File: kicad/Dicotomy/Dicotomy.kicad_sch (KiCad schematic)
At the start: 17 parts, among them J1 Conn_01x02_Pin, J2 Conn_01x04_Pin, J3 Conn_01x04_Socket, J4 Conn_01x02_Socket, Q1 Q_PNP, Q2 NPN, Q3 NPN, Q4 NPN, U1 WEMO S2 mini, U2 AC PWR SSR

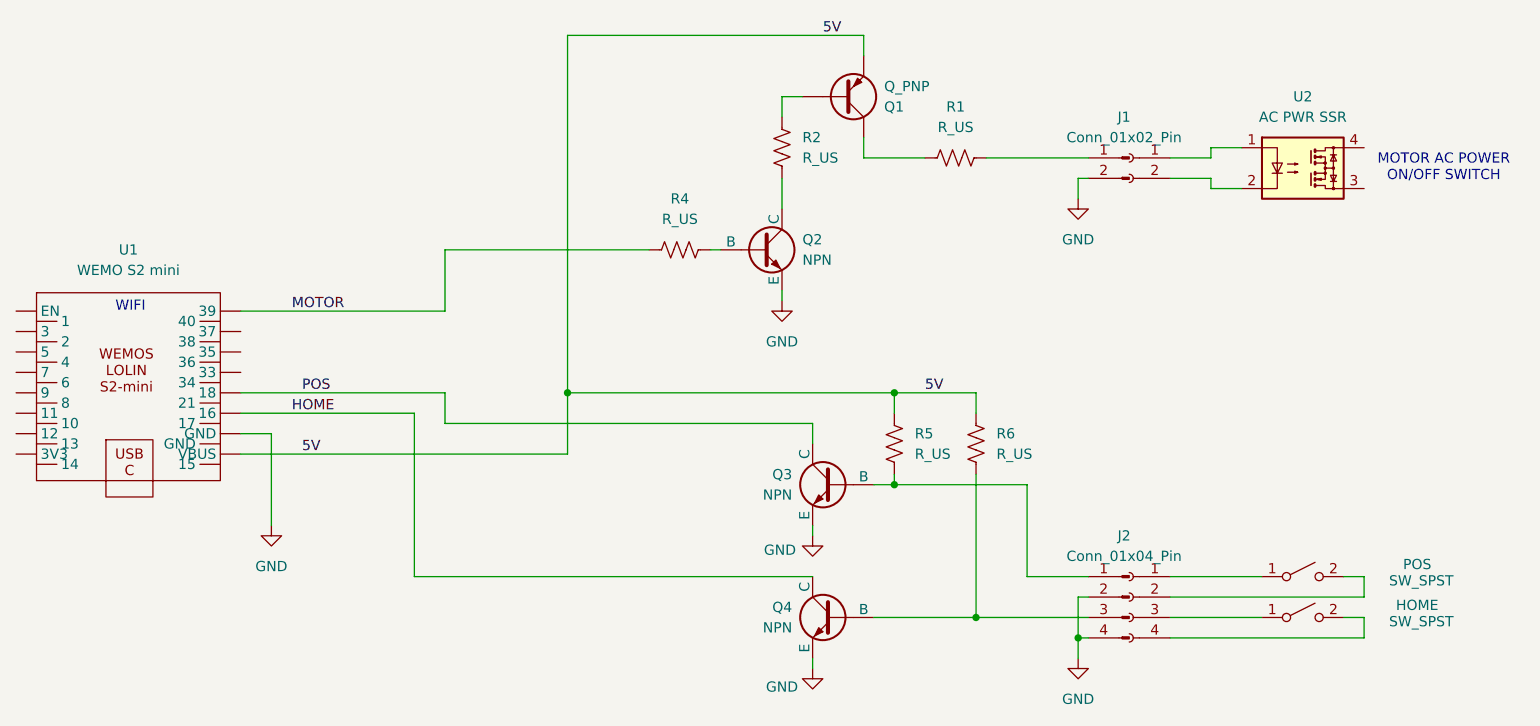
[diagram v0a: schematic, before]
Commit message: Update schematic with tran types and resistor values Created add_rotate.md requirements which are additions to the code_onoff.md requirements and used AI to create code_rotate.ino The basis of the code works, but fails to complete homing sequence on the bench while manually triggering switches, even with default home offset of 0 degrees. Added debug print statements TODO: Debug more
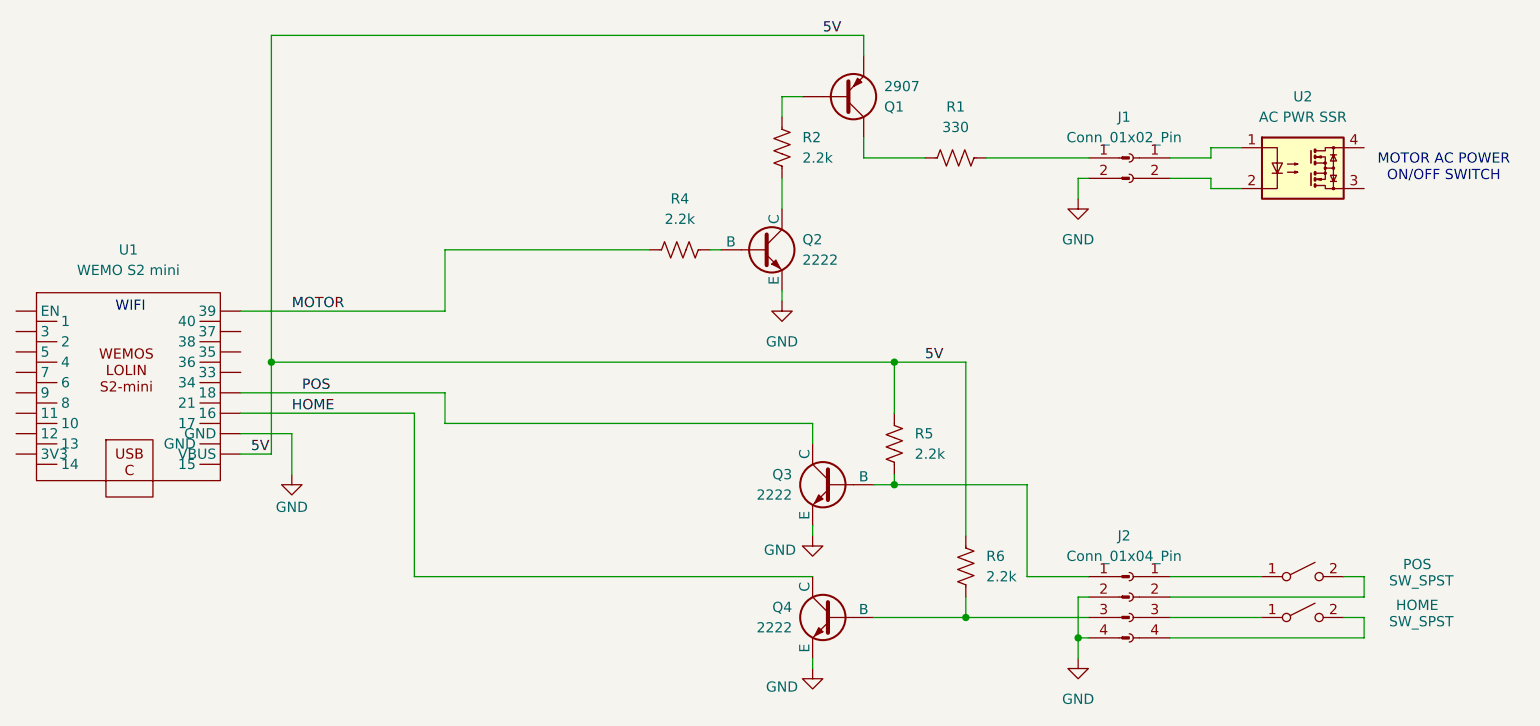
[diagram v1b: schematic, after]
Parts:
- Q1: value Q_PNP -> 2907
- Q2, Q3, Q4: value NPN -> 2222
- R1: value R_US -> 330
- R2, R4, R5, R6: value R_US -> 2.2k
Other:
- moved on the sheet: R6
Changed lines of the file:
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@@
 	)
 	(junction
-		(at 129.54 107.95)
+		(at 170.18 104.14)
 		(diameter 0)
 		(color 0 0 0 0)
 	)
 	(junction
-		(at 170.18 107.95)
+		(at 179.07 135.89)
 		(diameter 0)
 		(color 0 0 0 0)
 	)
 	(junction
-		(at 180.34 135.89)
+		(at 92.71 104.14)
 		(diameter 0)
 		(color 0 0 0 0)
@@
 	(wire
 		(pts
-			(xy 129.54 107.95) (xy 170.18 107.95)
-		)
-		(stroke
-			(width 0)
-			(type default)
-		)
-	)
-	(wire
-		(pts
 			(xy 226.06 135.89) (xy 228.6 135.89)
 		)
@@
 	(wire
 		(pts
-			(xy 129.54 63.5) (xy 166.37 63.5)
+			(xy 170.18 104.14) (xy 170.18 110.49)
+		)
+		(stroke
+			(width 0)
+			(type default)
+		)
+	)
+	(wire
+		(pts
+			(xy 92.71 63.5) (xy 166.37 63.5)
 		)
 		(stroke
@@
 	(wire
 		(pts
+			(xy 92.71 63.5) (xy 92.71 104.14)
+		)
+		(stroke
+			(width 0)
+			(type default)
+		)
+	)
+	(wire
+		(pts
 			(xy 193.04 81.28) (xy 193.04 83.82)
 		)
@@
 	(wire
 		(pts
-			(xy 170.18 107.95) (xy 180.34 107.95)
+			(xy 170.18 104.14) (xy 179.07 104.14)
 		)
 		(stroke
@@
 	(wire
 		(pts
-			(xy 170.18 107.95) (xy 170.18 110.49)
-		)
-		(stroke
-			(width 0)
-			(type default)
-		)
-	)
-	(wire
-		(pts
 			(xy 156.21 71.12) (xy 156.21 73.66)
 		)
@@
 	(wire
 		(pts
-			(xy 88.9 113.03) (xy 92.71 113.03)
+			(xy 88.9 113.03) (xy 95.25 113.03)
+		)
+		(stroke
+			(width 0)
+			(type default)
+		)
+	)
+	(wire
+		(pts
+			(xy 88.9 115.57) (xy 92.71 115.57)
 		)
 		(stroke
@@
 	(wire
 		(pts
-			(xy 180.34 118.11) (xy 180.34 135.89)
+			(xy 179.07 133.35) (xy 179.07 135.89)
 		)
 		(stroke
@@
 	(wire
 		(pts
+			(xy 92.71 104.14) (xy 92.71 115.57)
+		)
+		(stroke
+			(width 0)
+			(type default)
+		)
+	)
+	(wire
+		(pts
 			(xy 160.02 111.76) (xy 160.02 114.3)
 		)
@@
 	(wire
 		(pts
-			(xy 180.34 135.89) (xy 194.31 135.89)
+			(xy 179.07 135.89) (xy 194.31 135.89)
 		)
 		(stroke
@@
 	(wire
 		(pts
+			(xy 92.71 104.14) (xy 170.18 104.14)
+		)
+		(stroke
+			(width 0)
+			(type default)
+		)
+	)
+	(wire
+		(pts
 			(xy 204.47 138.43) (xy 228.6 138.43)
 		)
@@
 	(wire
 		(pts
-			(xy 92.71 113.03) (xy 92.71 124.46)
-		)
-		(stroke
-			(width 0)
-			(type default)
-		)
-	)
-	(wire
-		(pts
-			(xy 167.64 135.89) (xy 180.34 135.89)
-		)
-		(stroke
-			(width 0)
-			(type default)
-		)
-	)
-	(wire
-		(pts
-			(xy 129.54 63.5) (xy 129.54 107.95)
+			(xy 95.25 113.03) (xy 95.25 118.11)
+		)
+		(stroke
+			(width 0)
+			(type default)
+		)
+	)
+	(wire
+		(pts
+			(xy 167.64 135.89) (xy 179.07 135.89)
 		)
 		(stroke
@@
 	(wire
 		(pts
-			(xy 180.34 107.95) (xy 180.34 110.49)
+			(xy 179.07 104.14) (xy 179.07 125.73)
 		)
 		(stroke
@@
 	(wire
 		(pts
-			(xy 129.54 107.95) (xy 129.54 115.57)
-		)
-		(stroke
-			(width 0)
-			(type default)
-		)
-	)
-	(wire
-		(pts
 			(xy 156.21 95.25) (xy 156.21 96.52)
-		)
-		(stroke
-			(width 0)
-			(type default)
-		)
-	)
-	(wire
-		(pts
-			(xy 88.9 115.57) (xy 129.54 115.57)
 		)
 		(stroke
@@
 	)
 	(label "5V"
-		(at 173.99 107.95 0)
+		(at 90.17 115.57 0)
 		(effects
 			(font
@@
 		)
 	)
-	(label "HOME"
-		(at 95.25 110.49 0)
+	(label "5V"
+		(at 173.99 104.14 0)
 		(effects
 			(font
@@
 		)
 	)
-	(label "5V"
-		(at 96.52 115.57 0)
+	(label "HOME"
+		(at 95.25 110.49 0)
 		(effects
 			(font
@@
 	(symbol
 		(lib_id "power:GND")
-		(at 92.71 124.46 0)
+		(at 95.25 118.11 0)
 		(unit 1)
 		(exclude_from_sim no)
@@
 		(on_board yes)
 		(dnp no)
-		(fields_autoplaced yes)
 		(property "Reference" "#PWR01"
-			(at 92.71 130.81 0)
+			(at 95.25 124.46 0)
 			(effects
 				(font
@@
 		)
 		(property "Value" "GND"
-			(at 92.71 129.54 0)
+			(at 95.25 122.174 0)
 			(effects
 				(font
@@
 		)
 		(property "Footprint" ""
-			(at 92.71 124.46 0)
+			(at 95.25 118.11 0)
 			(effects
 				(font
@@
 		)
 		(property "Datasheet" ""
-			(at 92.71 124.46 0)
+			(at 95.25 118.11 0)
 			(effects
 				(font
@@
 		)
 		(property "Description" "Power symbol creates a global label with name \"GND\" , ground"
-			(at 92.71 124.46 0)
+			(at 95.25 118.11 0)
 			(effects
 				(font
@@
 			)
 		)
-		(property "Value" "R_US"
+		(property "Value" "2.2k"
 			(at 158.75 78.7399 0)
 			(effects
@@
 			)
 		)
-		(property "Value" "R_US"
+		(property "Value" "330"
 			(at 177.8 74.93 90)
 			(effects
@@
 			)
 		)
-		(property "Value" "NPN"
+		(property "Value" "2222"
 			(at 158.75 91.4399 0)
 			(effects
@@
 			)
 		)
-		(property "Value" "NPN"
+		(property "Value" "2222"
 			(at 157.48 120.6499 0)
 			(effects
@@
 			)
 		)
-		(property "Value" "R_US"
+		(property "Value" "2.2k"
 			(at 143.51 86.36 90)
 			(effects
@@
 			)
 		)
-		(property "Value" "Q_PNP"
+		(property "Value" "2907"
 			(at 168.91 69.8501 0)
 			(effects
@@
 			)
 		)
-		(property "Value" "R_US"
+		(property "Value" "2.2k"
 			(at 172.72 115.5699 0)
 			(effects
@@
 			)
 		)
-		(property "Value" "NPN"
+		(property "Value" "2222"
 			(at 157.48 137.1599 0)
 			(effects
@@
 	(symbol
 		(lib_id "Device:R_US")
-		(at 180.34 114.3 0)
+		(at 179.07 129.54 0)
 		(unit 1)
 		(exclude_from_sim no)
@@
 		(fields_autoplaced yes)
 		(property "Reference" "R6"
-			(at 182.88 113.0299 0)
+			(at 181.61 128.2699 0)
 			(effects
 				(font
@@
 			)
 		)
-		(property "Value" "R_US"
-			(at 182.88 115.5699 0)
+		(property "Value" "2.2k"
+			(at 181.61 130.8099 0)
 			(effects
 				(font
@@
 		)
 		(property "Footprint" ""
-			(at 181.356 114.554 90)
+			(at 180.086 129.794 90)
 			(effects
 				(font
@@
 		)
 		(property "Datasheet" "~"
-			(at 180.34 114.3 0)
+			(at 179.07 129.54 0)
 			(effects
 				(font
@@
 		)
 		(property "Description" "Resistor, US symbol"
-			(at 180.34 114.3 0)
-			(effects
-				(font
+			(at 179.07 129.54 0)
+			(effects
+				(font
